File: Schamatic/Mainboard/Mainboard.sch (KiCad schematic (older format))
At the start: 81 parts, among them J1 CONN_01X02, J10 CONN_01X04, J2 CONN_01X02, J3 CONN_01X02, J4 CONN_01X02, J5 CONN_01X02, J6 CONN_02X05, J7 CONN_02X20, J8 CONN_01X02, J9 CONN_01X02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

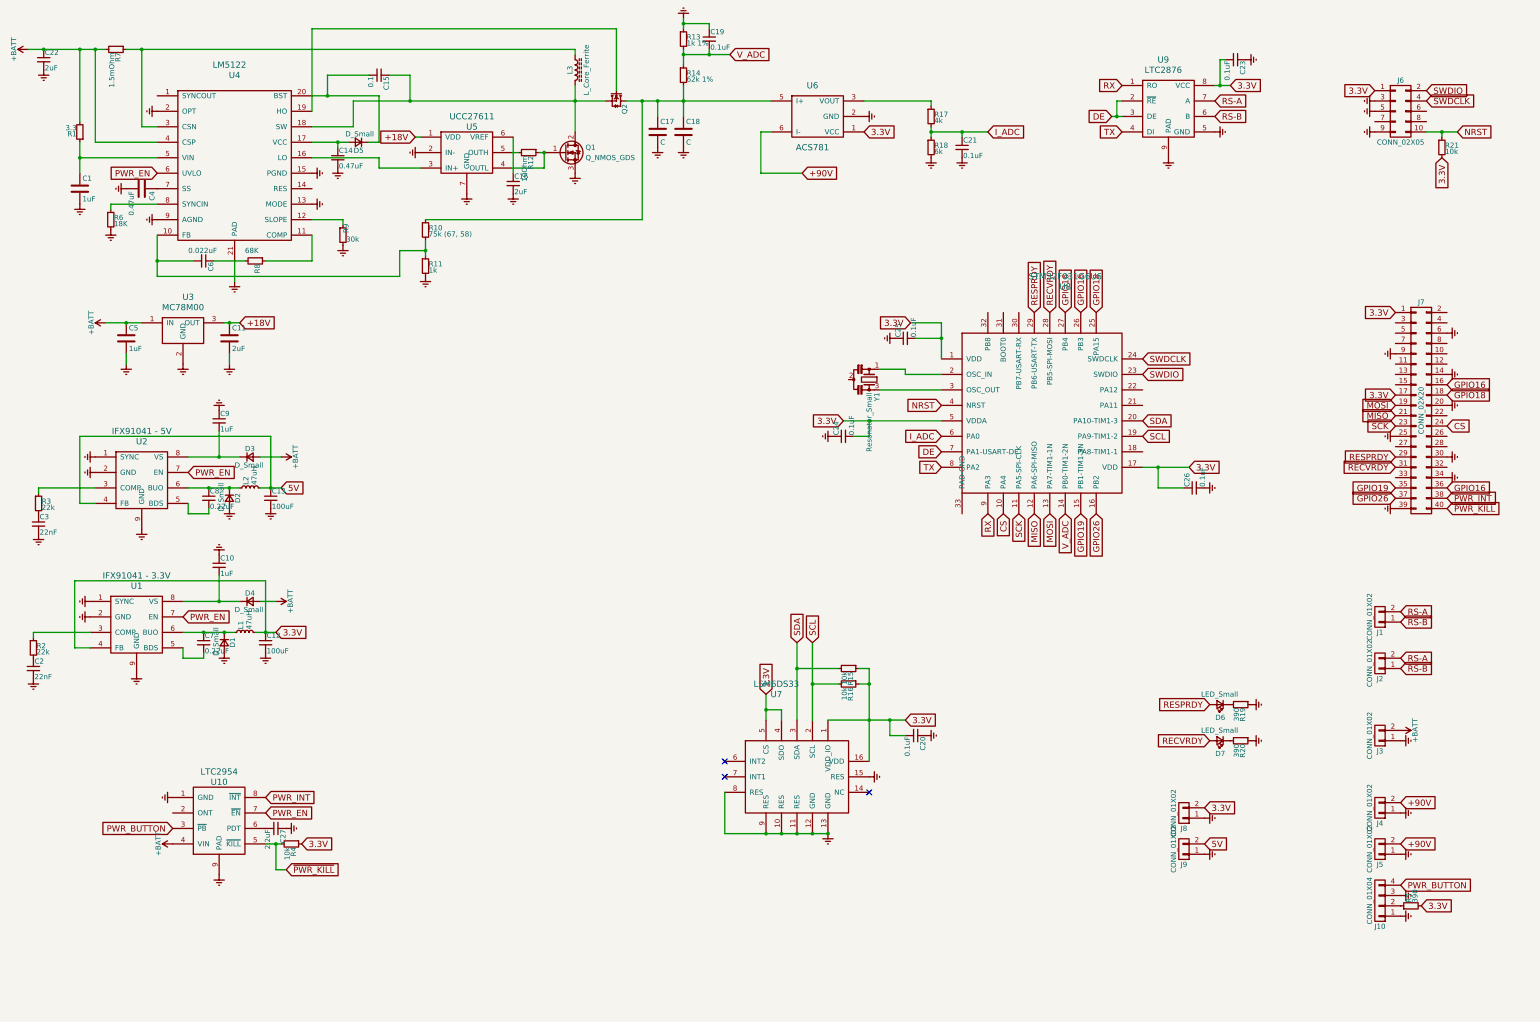
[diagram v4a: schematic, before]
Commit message: bigger current regulators
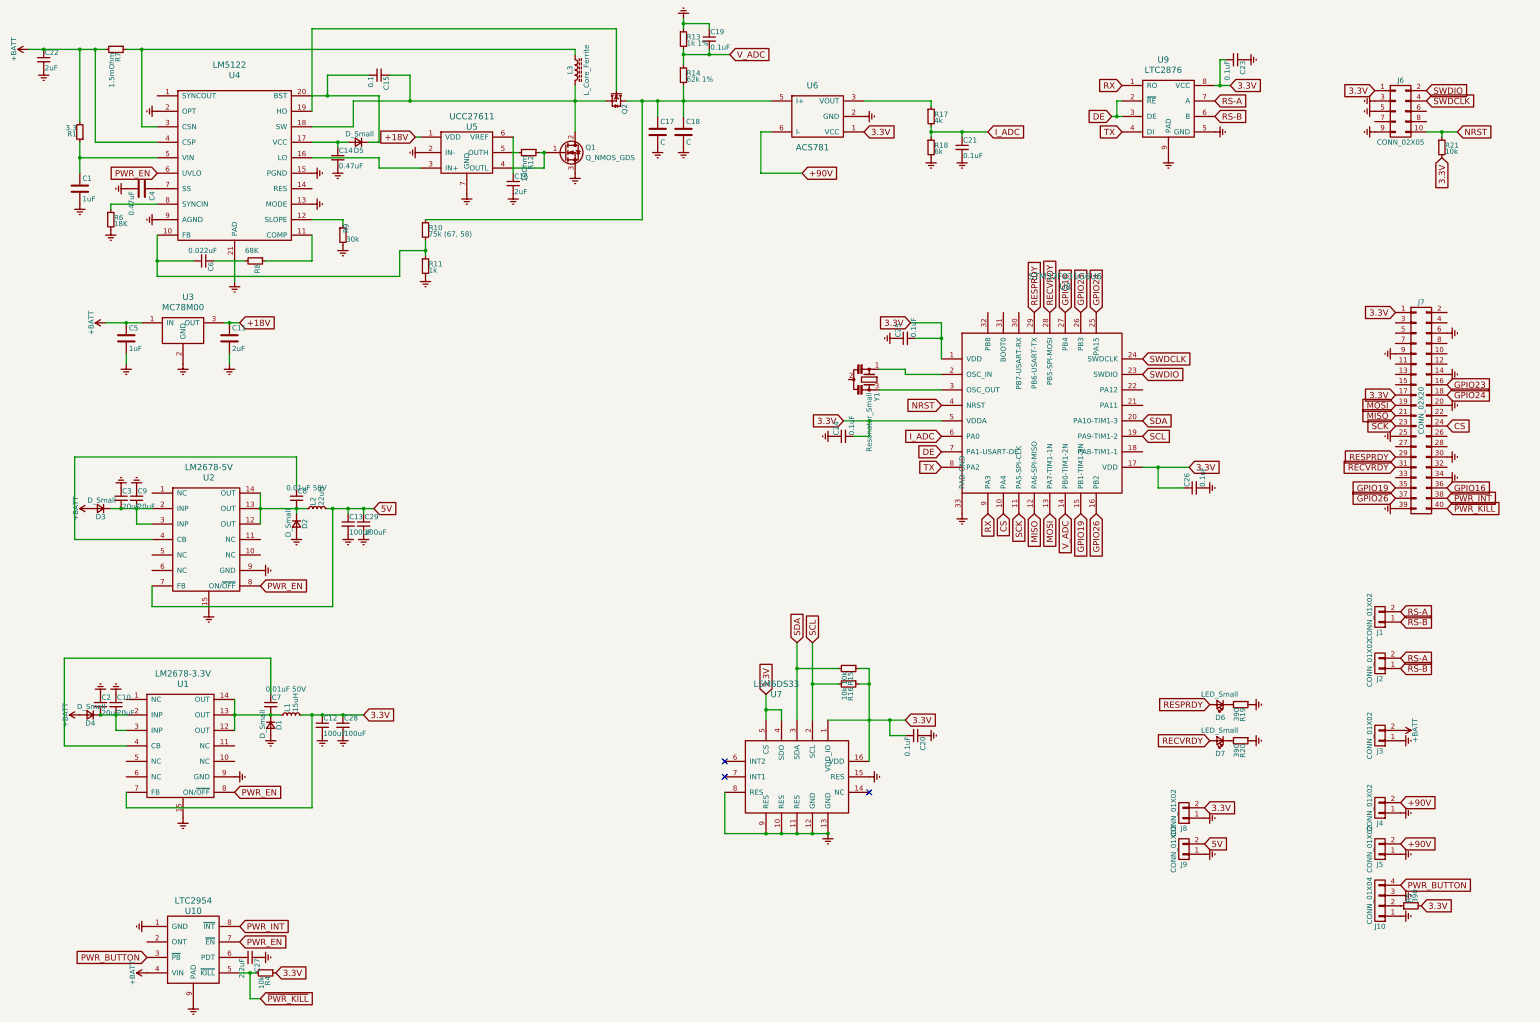
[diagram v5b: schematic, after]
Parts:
- removed R2, R3: 22k, Resistors_SMD:R_0603, symbol R_Small
- removed U1: IFX91041 - 3.3V, Housings_SOIC:HTSOP-8-1EP_3.9x4.9mm_Pitch1.27mm_ThermalVias, symbol IFX91041
- removed U2: IFX91041 - 5V, Housings_SOIC:HTSOP-8-1EP_3.9x4.9mm_Pitch1.27mm_ThermalVias, symbol IFX91041
- added C28, C29: 100uF, Capacitors_SMD:C_1206, symbol C_Small
- added U1: LM2678-3.3V, Dizzy:14-VSON, symbol LM2678
- added U2: LM2678-5V, Dizzy:14-VSON, symbol LM2678
- C10, C9: value 1uF -> 20uF; footprint Capacitors_SMD:C_0603 -> Capacitors_SMD:C_1210
- C2, C3: value 22nF -> 20uF; footprint Capacitors_SMD:C_0603 -> Capacitors_SMD:C_1210
- C7, C8: value 0.22uF -> 0.01uF 50V
- D1, D2, D3, D4: footprint Diodes_SMD:D_SOD-323 -> Diodes_SMD:D_SMA
- L1: value 47uH -> 15uH; footprint Inductors_SMD:L_1210 -> Inductors_SMD:L_10.4x10.4_H4.8
- L2: value 47uH -> 22uH; footprint Inductors_SMD:L_1210 -> Inductors_SMD:L_10.4x10.4_H4.8
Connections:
- net 3.3V: now also C28.1, U1.7 (FB)
- net 5V: now also C29.1, U2.7 (FB)
- net Earth: now also C2.1, C3.1, U8.33 (PAD-GND), C28.2, C29.2, U1.15, U1.9 (GND), U2.15, U2.9 (GND); no longer C2.2, C3.2
- net GPIO16: no longer J7.16 (P16), U8.26 (PB3)
- net PWR_EN: now also U1.8 (ON/~OFF), U2.8 (ON/~OFF)
- net at C8.2: now also D2.1 (K), L2.1, U2.12 (OUT), U2.13 (OUT), U2.14 (OUT)
- net at C9.2, D3.1 (K): now also C3.2, U2.2 (INP), U2.3 (INP)
- net at C7.2: now also D1.1 (K), L1.1, U1.12 (OUT), U1.13 (OUT), U1.14 (OUT)
- net at C10.2, D4.1 (K): now also C2.2, U1.2 (INP), U1.3 (INP)
- net GPIO18 renamed GPIO24
- new net: C8.1, U2.4 (CB)
- new net: C7.1, U1.4 (CB)
- new net GPIO23: J7.16 (P16), U8.26 (PB3)
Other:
- moved on the sheet: C10, C12, C13, C27, C7, C8, C9, D1, D2, D3, D4, L1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

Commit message: progress
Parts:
- C12, C13, C28, C29: footprint Capacitors_SMD:C_1206 -> Capacitors_SMD:C_1210
- C17, C18: value C -> 3.3uF
- C22: value 2uF -> 4.7uF
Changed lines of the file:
@@
 P 6850 1850
 F 0 "C17" H 6875 1950 50  0000 L CNN
-F 1 "C" H 6875 1750 50  0000 L CNN
+F 1 "3.3uF" H 6875 1750 50  0000 L CNN
 F 2 "Capacitors_SMD:C_1812" H 6888 1700 50  0001 C CNN
 F 3 "" H 6850 1850 50  0001 C CNN
@@
 P 7100 1850
 F 0 "C18" H 7125 1950 50  0000 L CNN
-F 1 "C" H 7125 1750 50  0000 L CNN
+F 1 "3.3uF" H 7125 1750 50  0000 L CNN
 F 2 "Capacitors_SMD:C_1812" H 7138 1700 50  0001 C CNN
 F 3 "" H 7100 1850 50  0001 C CNN
@@
 F 0 "C13" H 3860 5720 50  0000 L CNN
 F 1 "100uF" H 3860 5570 50  0000 L CNN
-F 2 "Capacitors_SMD:C_1206" H 3850 5650 50  0001 C CNN
+F 2 "Capacitors_SMD:C_1210" H 3850 5650 50  0001 C CNN
 F 3 "" H 3850 5650 50  0001 C CNN
 	1    3850 5650
@@
 F 0 "C12" H 3610 7670 50  0000 L CNN
 F 1 "100uF" H 3610 7520 50  0000 L CNN
-F 2 "Capacitors_SMD:C_1206" H 3600 7600 50  0001 C CNN
+F 2 "Capacitors_SMD:C_1210" H 3600 7600 50  0001 C CNN
 F 3 "" H 3600 7600 50  0001 C CNN
 	1    3600 7600
@@
 P 900 1150
 F 0 "C22" H 910 1220 50  0000 L CNN
-F 1 "2uF" H 910 1070 50  0000 L CNN
+F 1 "4.7uF" H 910 1070 50  0000 L CNN
 F 2 "Capacitors_SMD:C_1812" H 900 1150 50  0001 C CNN
 F 3 "" H 900 1150 50  0001 C CNN
@@
 F 0 "C29" H 4010 5720 50  0000 L CNN
 F 1 "100uF" H 4010 5570 50  0000 L CNN
-F 2 "Capacitors_SMD:C_1206" H 4000 5650 50  0001 C CNN
+F 2 "Capacitors_SMD:C_1210" H 4000 5650 50  0001 C CNN
 F 3 "" H 4000 5650 50  0001 C CNN
 	1    4000 5650
@@
 F 0 "C28" H 3810 7670 50  0000 L CNN
 F 1 "100uF" H 3810 7520 50  0000 L CNN
-F 2 "Capacitors_SMD:C_1206" H 3800 7600 50  0001 C CNN
+F 2 "Capacitors_SMD:C_1210" H 3800 7600 50  0001 C CNN
 F 3 "" H 3800 7600 50  0001 C CNN
 	1    3800 7600
@@
 GPIO23
 $Comp
-L Earth #PWR?
+L Earth #PWR078
 U 1 1 5B300A91
 P 9800 5550
-F 0 "#PWR?" H 9800 5300 50  0001 C CNN
+F 0 "#PWR078" H 9800 5300 50  0001 C CNN
 F 1 "Earth" H 9800 5400 50  0001 C CNN
 F 2 "" H 9800 5550 50  0001 C CNN

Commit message: changes
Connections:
- net Earth: now also Y1.2
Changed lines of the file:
@@
 	1    0    0    -1
 $EndComp
+$Comp
+L Earth #PWR?
+U 1 1 5B3F6BBE
+P 8700 4250
+F 0 "#PWR?" H 8700 4000 50  0001 C CNN
+F 1 "Earth" H 8700 4100 50  0001 C CNN
+F 2 "" H 8700 4250 50  0001 C CNN
+F 3 "" H 8700 4250 50  0001 C CNN
+	1    8700 4250
+	0    1    1    0
+$EndComp
 $EndSCHEMATC

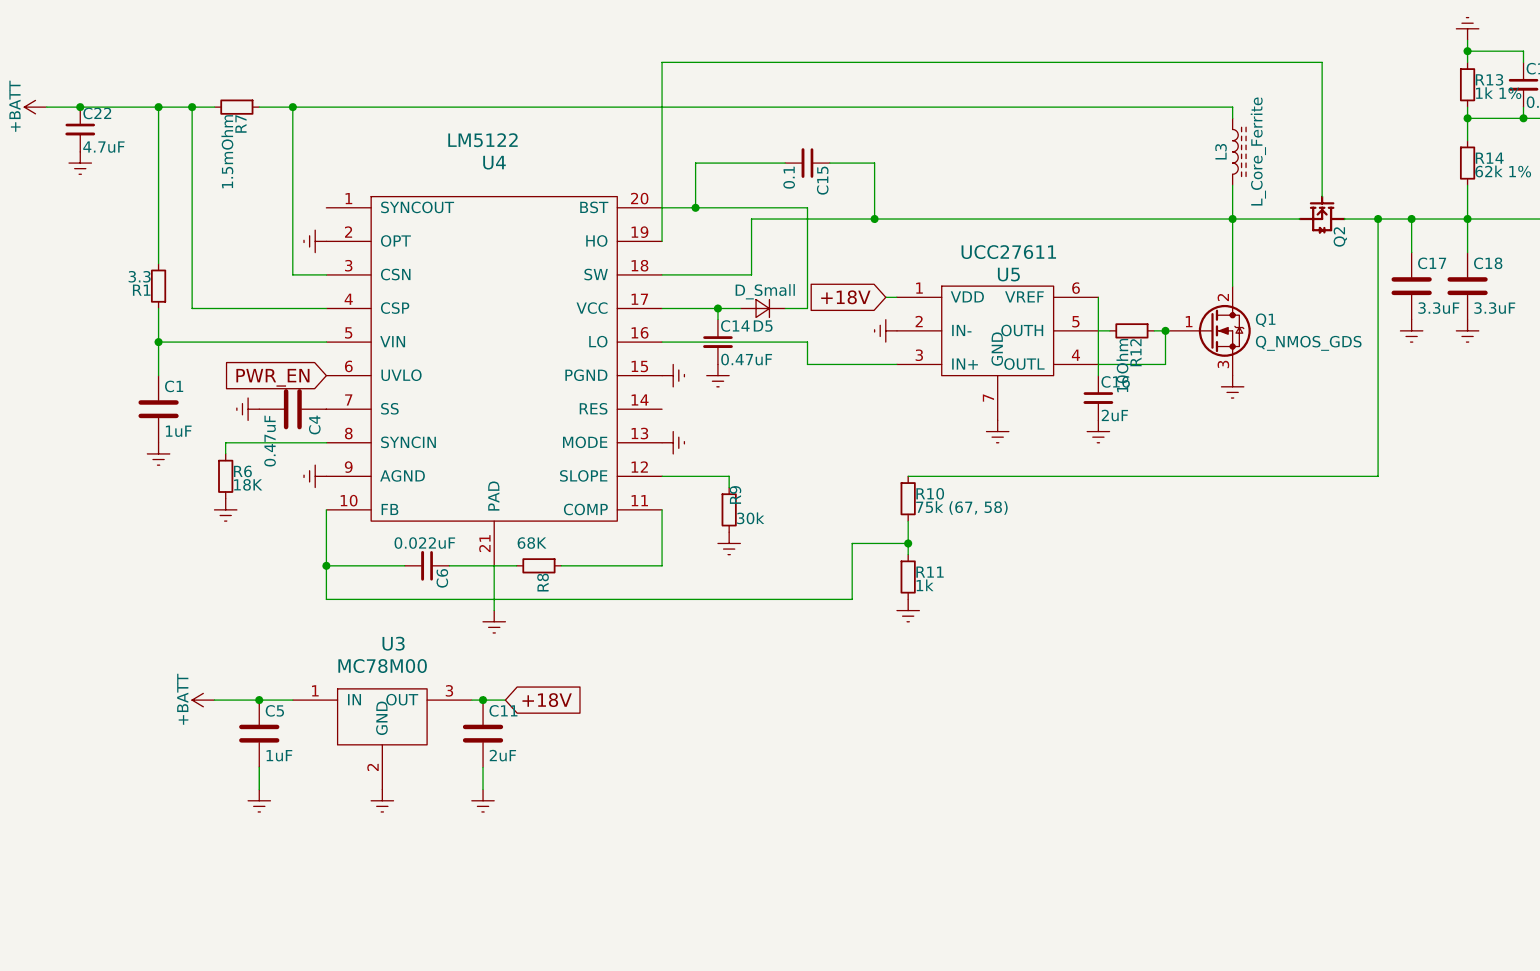
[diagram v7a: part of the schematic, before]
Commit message: mainboard plain MOSFETS
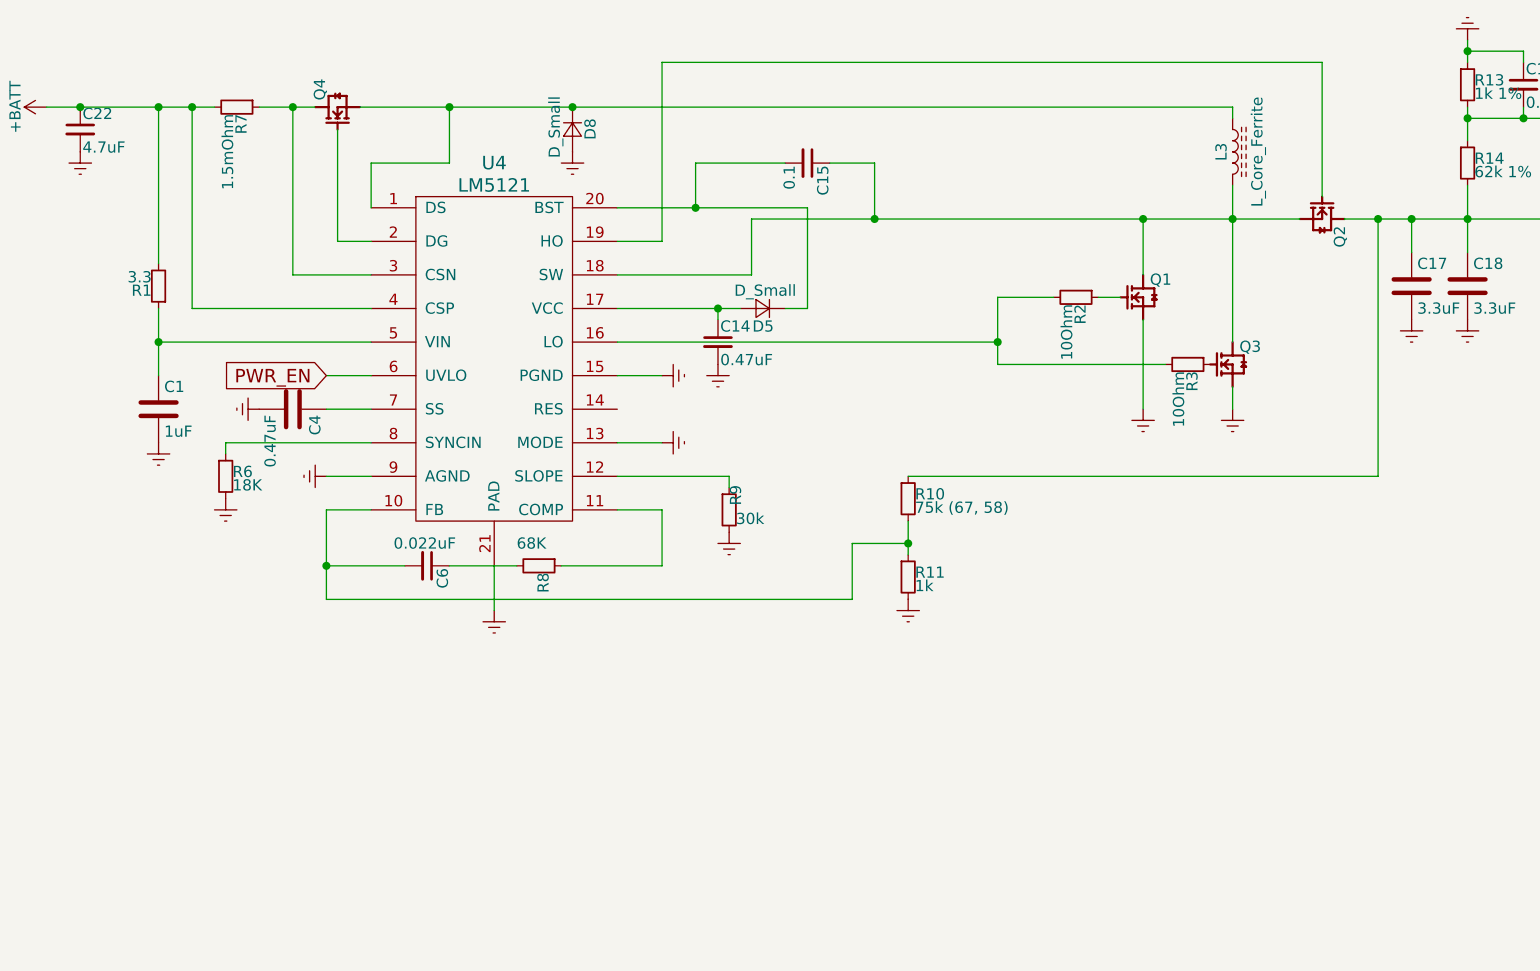
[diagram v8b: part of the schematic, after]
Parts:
- removed C11: 2uF, Capacitors_SMD:C_0805, symbol C
- removed C16: 2uF, Capacitors_SMD:C_0603, symbol C_Small
- removed C5: 1uF, Capacitors_SMD:C_0603, symbol C
- removed Q1: Q_NMOS_GDS, Dizzy:EPC2022, symbol Q_NMOS_GDS
- removed R12: 10Ohm, Resistors_SMD:R_0603, symbol R_Small
- removed U3: MC78M00, TO_SOT_Packages_SMD:TO-252-2, symbol MC78M00
- removed U4: LM5122, Housings_SSOP:HTSSOP-20-1EP_4.4x6.5mm_Pitch0.65mm_ThermalPad, symbol LM5122
- removed U5: UCC27611, Housings_DFN_QFN:DFN-6-1EP_2x2mm_Pitch0.65mm, symbol UCC27611
- added D8: D_Small, Diodes_SMD:D_SMA, symbol D_Small
- added Q1, Q3, Q4: PSMN014-40YS, Dizzy:PSMN3R3-40YS, symbol PSMN014-40YS
- added R2, R3: 10Ohm, Resistors_SMD:R_0603, symbol R_Small
- added U4: LM5121, Housings_SSOP:HTSSOP-20-1EP_4.4x6.5mm_Pitch0.65mm_ThermalPad, symbol LM5121
- J7: footprint Pin_Headers:Pin_Header_Straight_2x20_Pitch2.54mm_SMD -> Pin_Headers:Pin_Header_Straight_2x20_Pitch2.54mm
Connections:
- net +BATT: now also U4.4 (CSP)
- net Earth: now also D8.2 (A), Q1.1 (S), Q1.2 (S), Q1.3 (S), Q3.1 (S), Q3.2 (S), Q3.3 (S), U4.13 (MODE), U4.15 (PGND), U4.21 (PAD), U4.9 (AGND)
- net PWR_EN: now also U4.6 (UVLO)
- net at C6.2, R10.2, R11.1: now also U4.10 (FB)
- net at R8.1: now also U4.11 (COMP)
- net at R9.1: now also U4.12 (SLOPE)
- net at C14.1, D5.2 (A): now also U4.17 (VCC)
- net at C15.1, L3.2, Q2.1 (S)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: now also Q1.5678 (D), Q3.5678 (D), U4.18 (SW)
- net at Q2.4 (G): now also U4.19 (HO)
- net at C15.2, D5.1 (K): now also U4.20 (BST)
- net at L3.1: now also D8.1 (K), Q4.1 (S), Q4.2 (S), Q4.3 (S), U4.1 (DS); no longer R7.1
- net at C1.1, R1.1: now also U4.5 (VIN)
- net at C4.1: now also U4.7 (SS)
- net at R6.1: now also U4.8 (SYNCIN)
- new net: Q4.5678 (D), R7.1, U4.3 (CSN)
- new net: Q1.4 (G), R2.1
- new net: Q3.4 (G), R3.1
- new net: R2.2, R3.2, U4.16 (LO)
- new net: Q4.4 (G), U4.2 (DG)
